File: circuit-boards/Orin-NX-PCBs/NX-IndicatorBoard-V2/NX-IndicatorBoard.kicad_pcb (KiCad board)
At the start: 6 copper layers, 107.4 x 79 mm, 44 parts, among them J1 NX Expansion, J2 CAN1, J3 CAN1, J4 CAN2, J5 CAN2, J6 PC LED, U1 74LVC245ABQ, U2 MCP2558FD, U3 MCP2518FDT-H/SL, U4 40MHz, U5 MCP2558FD, U6 MCP2518FDT-H/SL, U7 40MHz

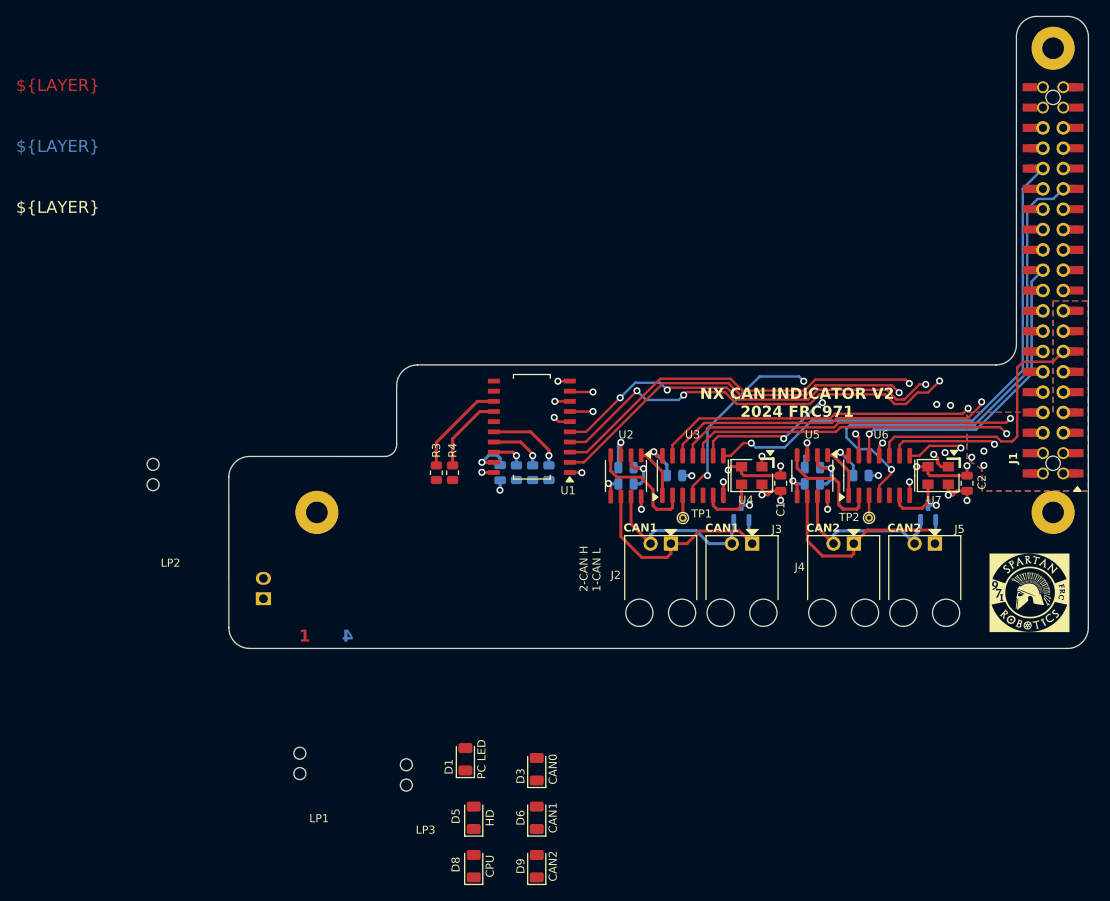
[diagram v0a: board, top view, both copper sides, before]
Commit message: Checkin of NX Indicator board 2x CAN FD + 6 LEDs
Signed-off-by: Scott <sgberman1@gmail.com>
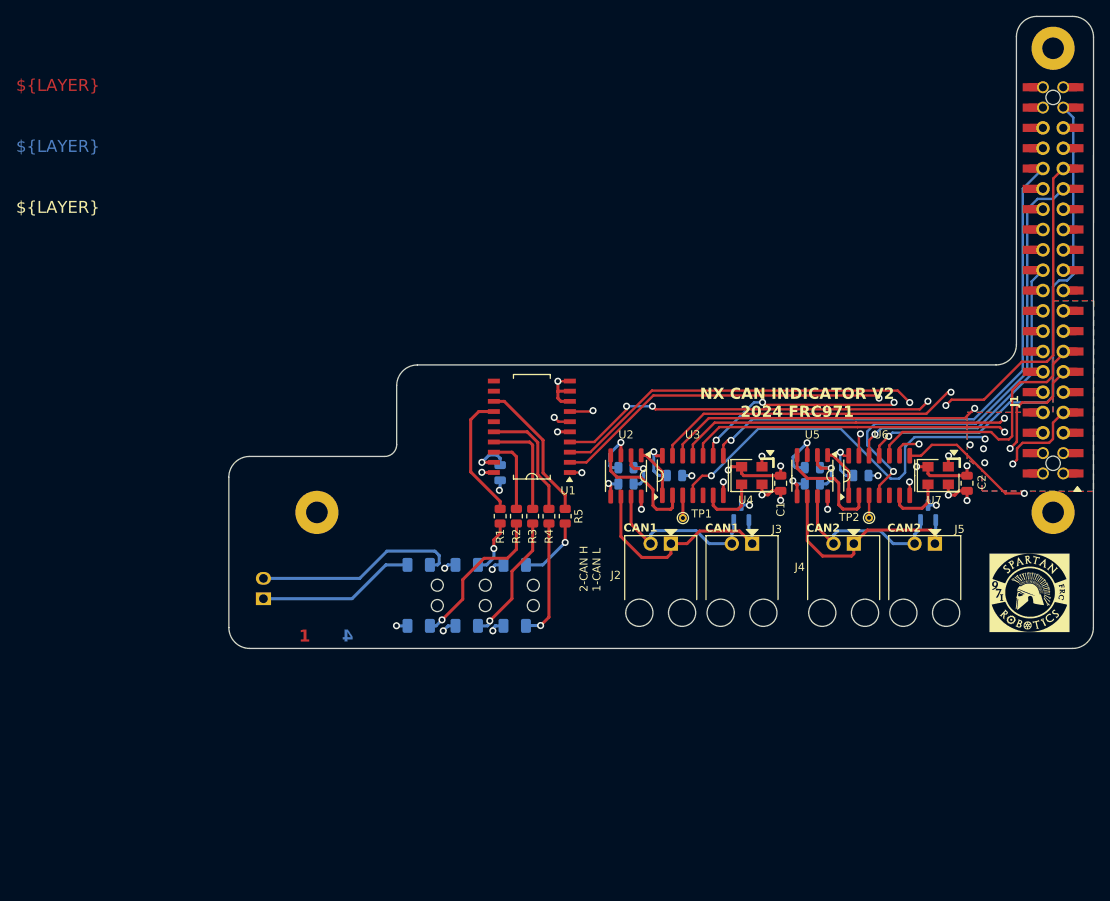
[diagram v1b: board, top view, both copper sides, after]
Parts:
- D3: renamed from D8; moved to B.Cu
- D4: renamed from D5; moved to B.Cu
- D5: renamed from D1; moved to B.Cu
- D6: renamed from D9; moved to B.Cu
- D7: renamed from D6; moved to B.Cu
- D8: renamed from D3; moved to B.Cu
- LP1: renamed from LP3; moved to B.Cu
- LP2: moved to B.Cu
- LP3: renamed from LP1; moved to B.Cu
- R2: renamed from R8; moved to F.Cu
- R3: renamed from R7; moved to F.Cu
- R4: renamed from R6; moved to F.Cu
- moved LP2 40.0 mm to (84.8, 126.0), turned to 180 degrees
- moved D3 38.0 mm to (90.7, 115.6), turned to 0 degrees
- moved D4 31.6 mm to (84.7, 115.6), turned to 0 degrees
- moved D6 30.2 mm to (90.7, 123.2), turned to 0 degrees
- moved D7 25.5 mm to (84.7, 123.2), turned to 0 degrees
- moved LP1 25.2 mm to (90.8, 126.0), turned to 180 degrees
- moved D5 25.0 mm to (78.7, 115.6), turned to 0 degrees
- moved LP3 24.5 mm to (78.8, 126.0), turned to 180 degrees
- moved D8 23.2 mm to (78.7, 123.2), turned to 0 degrees
- moved R5 17.0 mm to (97.0, 109.5)
- moved R1 8.05 mm to (88.9, 109.5)
- moved R2 5.44 mm to (90.9, 109.5)
- moved R3 5.44 mm to (93.0, 109.5)
- moved R4 5.44 mm to (95.0, 109.5)
- renumbered D10 to D1, D11 to D2, H2 to H1, H3 to H2, H5 to H3, R4 to R1, R3 to R5
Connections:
- U1 pad 5: /UART1_RTS -> GND
- U1 pad 6: /I2S0_DIN -> /UART1_RTS
- U1 pad 8: /I2S0_DOUT -> GND
- U1 pad 9: /I2S0_FS -> GND
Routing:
- net /I2S0_FS: track 106.2 -> 1.64 mm, vias 1 -> 0
- net /I2S0_DIN: track 100.4 -> 1.64 mm, vias 1 -> 0
- net /I2S0_DOUT: track 98.2 -> 1.64 mm, vias 1 -> 0
- net /NX_PC_LED+: track 0.00 -> 25.8 mm
- net /UART1_CTS: track 111.1 -> 90.9 mm
- net /NX_PC_LED-: track 0.00 -> 19.8 mm
- net Net-(D8-A): track 0.00 -> 19.4 mm, vias 0 -> 1
- net Net-(D7-A): track 0.00 -> 16.3 mm, vias 0 -> 1
- net GND: track 64.6 -> 79.6 mm, vias 17 -> 23
- net Net-(D6-A): track 0.00 -> 15.0 mm, vias 0 -> 1
- net /UART1_RTS: track 69.7 -> 84.2 mm, vias 3 -> 2
- net Net-(D3-A): track 0.00 -> 8.43 mm, vias 0 -> 1
- net Net-(D4-A): track 0.00 -> 6.96 mm, vias 0 -> 1
- net /SPI1_MOSI: track 59.2 -> 65.4 mm
- net Net-(U1-B4): track 9.90 -> 16.0 mm
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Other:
- board size 107.4 x 79 mm -> 108.1 x 79 mm
- copper layers 6 -> 4
- board text added: "108.0598 mm x 78.9830 mm"
- board text removed: "107.4248 mm x 79.0000 mm"

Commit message: Fix bom. Made LVC245 an SO-20 part
Signed-off-by: Scott Berman <scott.berman@bluerivertech.com>
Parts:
- U1: value 74LVC245ABQ -> 74LVC245AD
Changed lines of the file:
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@@
 			)
 		)
-		(property "Value" "74LVC245ABQ"
+		(property "Value" "74LVC245AD"
 			(at 0 7.99 180)
 			(layer "F.Fab")
@@
 			)
 		)
-		(property "MFG P/N" "74LVC245ABQ,115"
+		(property "MFG P/N" "74LVC245AD,118"
 			(at 0 0 180)
 			(unlocked yes)
@@
 			)
 		)
-		(property "DIST P/N" "1727-3495-1-ND"
+		(property "DIST P/N" "1727-3104-1-ND"
 			(at 0 0 180)
 			(unlocked yes)
@@
 		(fp_arc
 			(start 0.762262 -2.56)
-			(mid 0.010001 -1.797803)
+			(mid 0.010001 -1.797804)
 			(end -0.762 -2.54)
 			(stroke
@@
 		(height 14.673321)
 		(orientation 0)
-		(gr_text "4253.9 mils"
+		(gr_text "108.0 mm"
 			(at 223.8836 167.6838 0)
 			(layer "User.1")
@@
 		(height -15.0042)
 		(orientation 1)
-		(gr_text "2953.1 mils"
+		(gr_text "75.0 mm"
 			(at 156.3046 119.2551 90)
 			(layer "User.1")
@@
 		(height 9.999721)
 		(orientation 0)
-		(gr_text "3874.6 mils"
+		(gr_text "98.4 mm"
 			(at 219.0814 163.0016 0)
 			(layer "User.1")
@@
 		(height -4.6918)
 		(orientation 1)
-		(gr_text "669.3 mils"
+		(gr_text "17.0 mm"
 			(at 166.617 148.2594 90)
 			(layer "User.1")
@@
 		(height 12.311121)
 		(orientation 0)
-		(gr_text "4055.1 mils"
+		(gr_text "103.0 mm"
 			(at 221.3588 165.3216 0)
 			(layer "User.1")
@@
 		(height 8.221721)
 		(orientation 0)
-		(gr_text "825.6 mils"
+		(gr_text "21.0 mm"
 			(at 180.34415 161.2322 0)
 			(layer "User.1")
@@
 		(height -7.9938)
 		(orientation 1)
-		(gr_text "944.6 mils"
+		(gr_text "24.0 mm"
 			(at 163.315 144.7626 90)
 			(layer "User.1")
@@
 		(height 5.554721)
 		(orientation 0)
-		(gr_text "433.1 mils"
+		(gr_text "11.0 mm"
 			(at 175.3588 158.5652 0)
 			(layer "User.1")
@@
 		(height -18.8904)
 		(orientation 1)
-		(gr_text "3109.9 mils"
+		(gr_text "79.0 mm"
 			(at 152.4184 117.2636 90)
 			(layer "User.1")
@@
 		(height -11.3466)
 		(orientation 1)
-		(gr_text "1394.9 mils"
+		(gr_text "35.4 mm"
 			(at 159.9622 139.0444 90)
 			(layer "User.1")

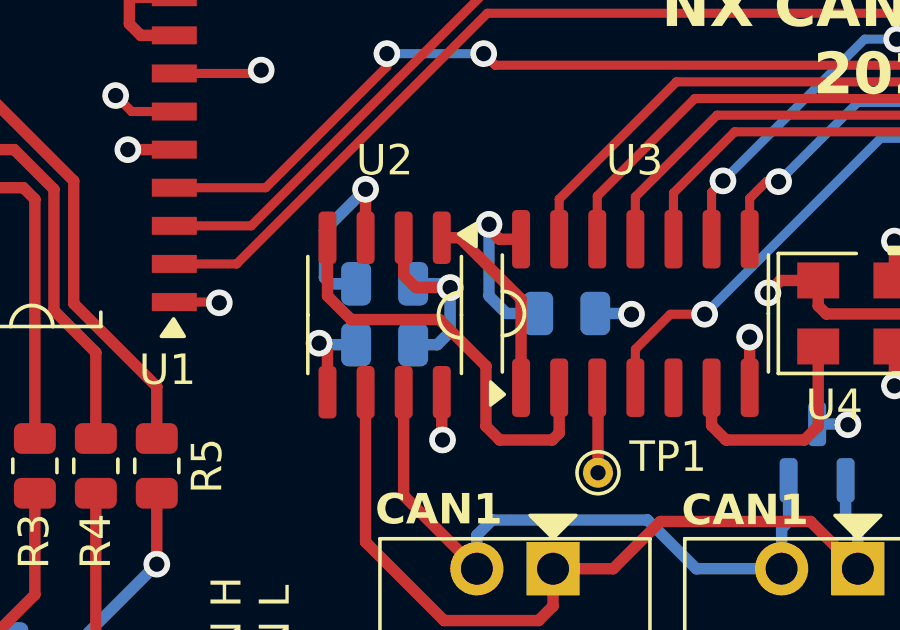
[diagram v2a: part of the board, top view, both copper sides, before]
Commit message: Minor BOM fix
Signed-off-by: Scott Berman <scott.berman@bluerivertech.com>
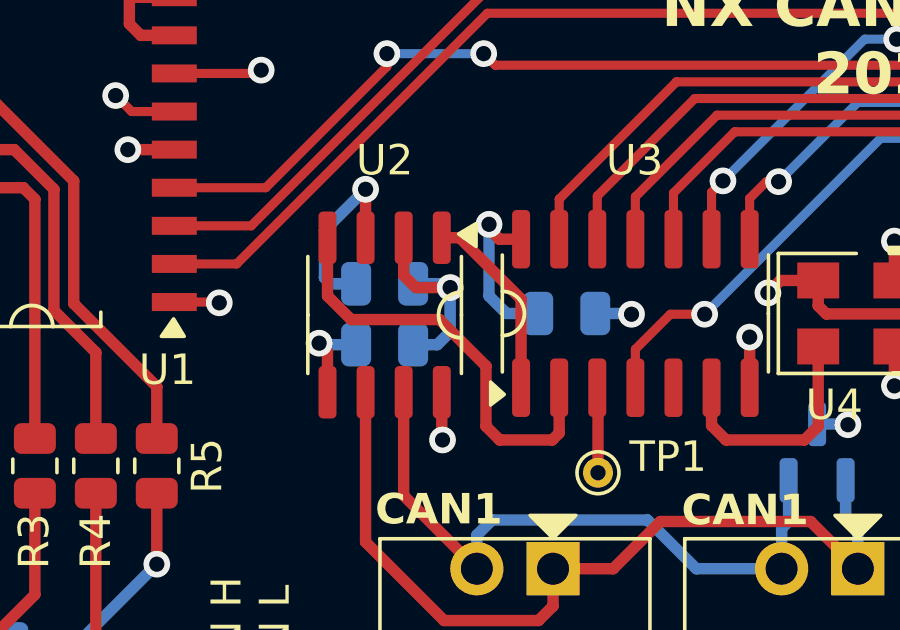
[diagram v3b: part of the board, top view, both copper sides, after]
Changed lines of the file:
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@@
 			)
 		)
-		(property "MFG P/N" "70555-0036"
+		(property "MFG P/N" "0705550036"
 			(at 0 0 -90)
 			(unlocked yes)
@@
 		(fp_arc
 			(start 0.762262 -2.56)
-			(mid 0.010001 -1.797804)
+			(mid 0.010001 -1.797805)
 			(end -0.762 -2.54)
 			(stroke
@@
 			)
 		)
-		(property "MFG P/N" "70555-0036"
+		(property "MFG P/N" "0705550036"
 			(at 0 0 -90)
 			(unlocked yes)
